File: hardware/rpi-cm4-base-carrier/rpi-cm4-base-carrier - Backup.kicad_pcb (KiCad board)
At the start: 4 copper layers, 129.5 x 61.3 mm, 66 parts, among them J1 690-019-298-412, J2 DNP, J3 USB4105-GF-A, J4 SM04B-SRSS-TB(LF)(SN), J5 THD-02-R, J6 Micro_SD_Card_Det, J7 USB_OTG, J8 690-008-221-904, J9 Conn_02x05_Odd_Even, U1 RT9742SNGV, U10 AP22653W6, U2 74LVC1G07SE-7, U3 TPD4EUSB30, U4 TPD4EUSB30, U5 MagJack-A70-112-331N126, U6 RT9742GGJ5, U7 FSUSB42MUX, U8 USB2514B-I/M2, U9 TPD4EUSB30, Y1 CX3225CA24000D0HSSCC

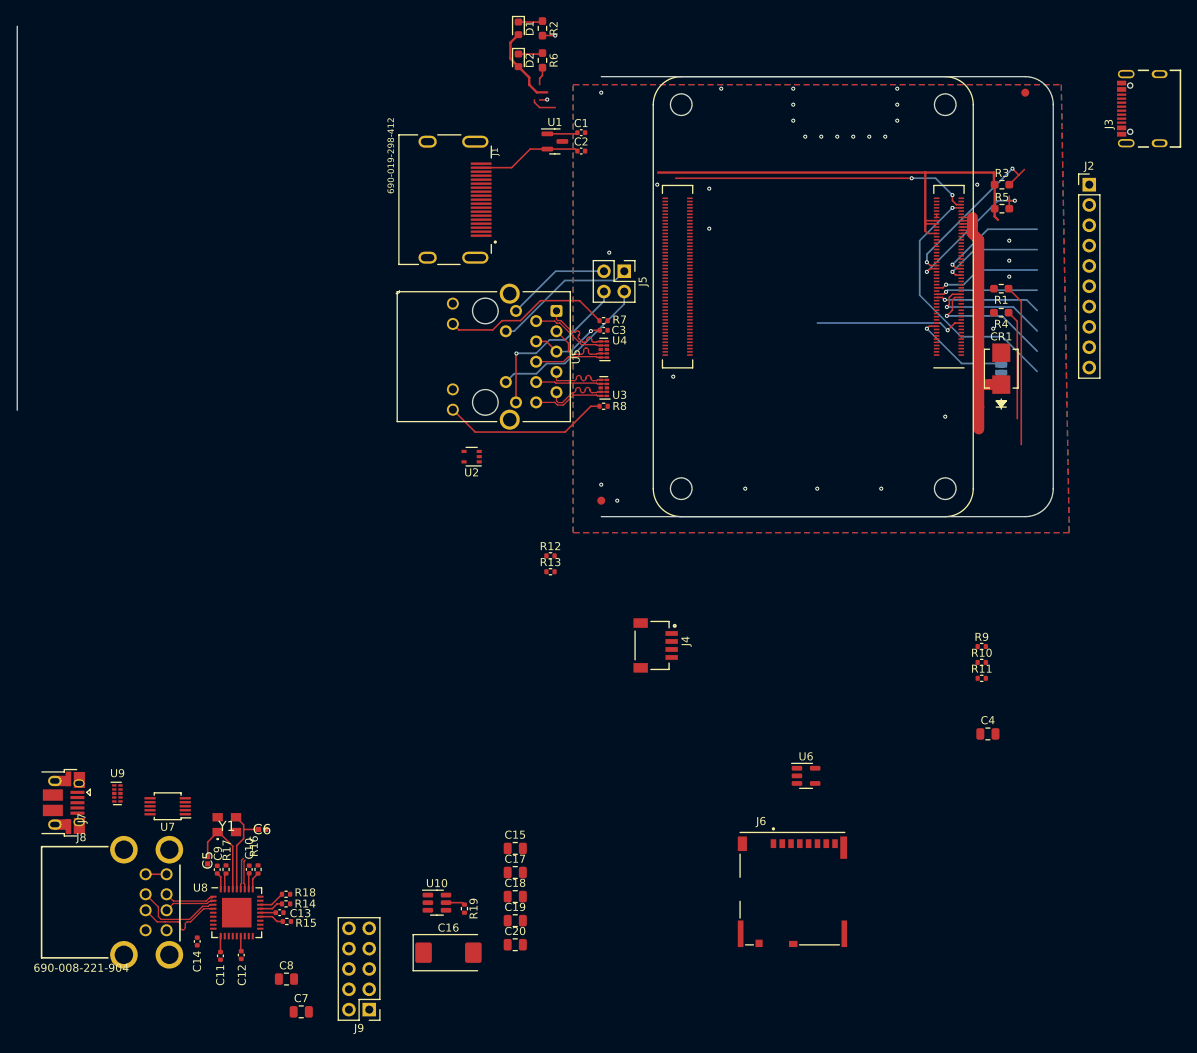
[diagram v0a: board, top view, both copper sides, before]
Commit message: routing for some modules progressing quickly, USBHUB mostly complete, thought needed regarding which connectors should be exposed post assembly and which should be for internal use only. LED identifiers and buttons still missing
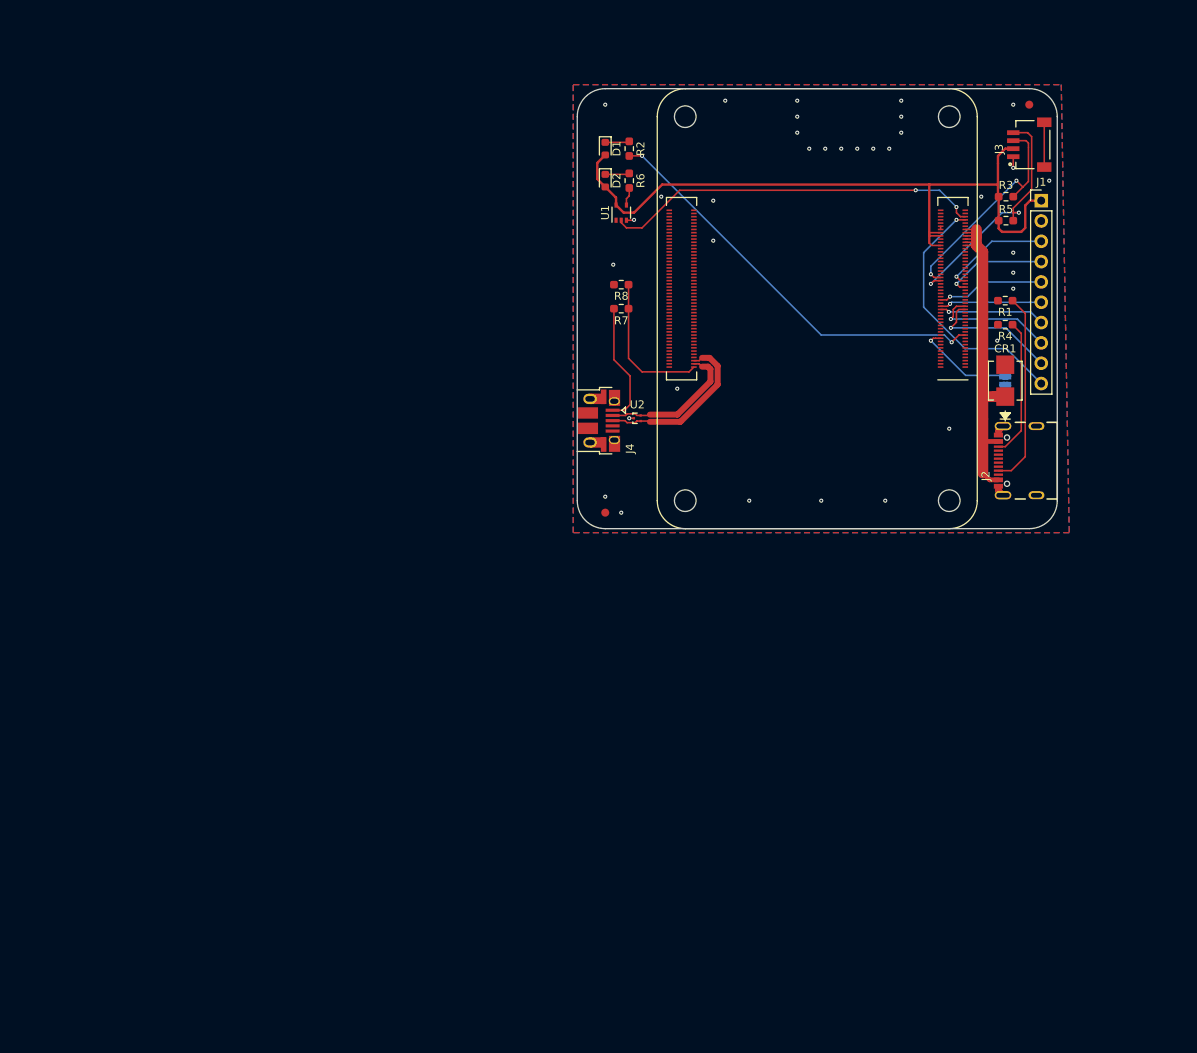
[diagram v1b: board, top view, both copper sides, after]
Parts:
- removed C1, C10, C11, C12, C13, C14, C2, C3, C9: 100n, Capacitor_SMD:C_0402_1005Metric
- removed C15, C17, C18, C19, C20, C4, C7, C8: 10u, Capacitor_SMD:C_0805_2012Metric
- removed C16: 100uF, Capacitor_Tantalum_SMD:CP_EIA-7343-31_Kemet-D
- removed C5, C6: 8pf, SamacSys_Parts:CAPC1005X56N
- removed J5: THD-02-R, Connector_PinHeader_2.54mm:PinHeader_2x02_P2.54mm_Vertical
- removed J6: Micro_SD_Card_Det, CM4IO:SDCARD_MOLEX_503398-1892
- removed J7: USB_OTG, CM4IO:USB_Micro-B_EDAC_UCON00686
- removed J8: 690-008-221-904, CM4IO:MOLEX_USB_67298-4090
- removed J9: Conn_02x05_Odd_Even, Connector_PinHeader_2.54mm:PinHeader_2x05_P2.54mm_Vertical
- removed R10, R9: nf, Resistor_SMD:R_0402_1005Metric
- removed R11, R17: 12K 1%, Resistor_SMD:R_0402_1005Metric
- removed R12, R13: 2.2K 1%, Resistor_SMD:R_0402_1005Metric
- removed R14, R15, R16, R18: 36K 1%, Resistor_SMD:R_0402_1005Metric
- removed R19: 15K 1%, Resistor_SMD:R_0402_1005Metric
- removed U10: AP22653W6, Package_TO_SOT_SMD:SOT-23-6
- removed U3, U4, U9: TPD4EUSB30, Package_SON:USON-10_2.5x1.0mm_P0.5mm
- removed U5: MagJack-A70-112-331N126, CM4IO:TRJG0926HENL
- removed U6: RT9742GGJ5, Package_TO_SOT_SMD:SOT-23-5
- removed U7: FSUSB42MUX, Package_SO:MSOP-10_3x3mm_P0.5mm
- removed U8: USB2514B-I/M2, Package_DFN_QFN:QFN-36-1EP_6x6mm_P0.5mm_EP3.7x3.7mm
- removed Y1: CX3225CA24000D0HSSCC, SamacSys_Parts:CX3225CA24000D0HSSCC
- J1: value 690-019-298-412 -> DNP; footprint CM4IO:EDAC 690-019-298-412 -> Connector_PinHeader_2.54mm:PinHeader_1x10_P2.54mm_Vertical
- J2: value DNP -> USB4105-GF-A; footprint Connector_PinHeader_2.54mm:PinHeader_1x10_P2.54mm_Vertical -> USB4105-GF-A:GCT_USB4105-GF-A
- J3: value USB4105-GF-A -> SM04B-SRSS-TB(LF)(SN); footprint USB4105-GF-A:GCT_USB4105-GF-A -> SM04B-SRSS-TB_LF__SN_:JST_SM04B-SRSS-TB(LF)(SN)
- J4: value SM04B-SRSS-TB(LF)(SN) -> USB_OTG; footprint SM04B-SRSS-TB_LF__SN_:JST_SM04B-SRSS-TB(LF)(SN) -> CM4IO:USB_Micro-B_EDAC_UCON00686
- R7, R8: value 470R -> 2.2K 1%; footprint Resistor_SMD:R_0402_1005Metric -> Resistor_SMD:R_0603_1608Metric_Pad0.98x0.95mm_HandSolder
- U1: value RT9742SNGV -> 74LVC1G07SE-7; footprint Package_TO_SOT_SMD:SOT-23 -> Package_TO_SOT_SMD:SOT-353_SC-70-5
- U2: value 74LVC1G07SE-7 -> TPD2EUSB30; footprint Package_TO_SOT_SMD:SOT-353_SC-70-5 -> Package_TO_SOT_SMD:Texas_DRT-3
- moved J1 70.7 mm to (174.5, 92.5), turned to 0 degrees
- moved J2 35.1 mm to (173.9, 125.0), turned to 90 degrees
- moved J4 29.9 mm to (118.1, 120.0)
- moved U2 21.2 mm to (124.0, 119.7), turned to 90 degrees
- moved J3 18.8 mm to (171.0, 85.5)
- moved D1 18.5 mm to (120.0, 86.0)
- moved D2 18.5 mm to (120.0, 90.0)
- moved R2 18.5 mm to (123.0, 86.0)
- moved R6 18.5 mm to (123.0, 90.0)
- moved R8 15.4 mm to (122.0, 103.0), turned to 180 degrees
- moved U1 12.2 mm to (122.0, 94.0), turned to 90 degrees
- moved R7 2.66 mm to (122.0, 106.0)
- moved CR1 1.58 mm to (170.0, 115.0)
- moved JP1 1.58 mm to (170.0, 115.0)
- moved Module1 1.58 mm to (163.0, 82.0)
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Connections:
- net /CM4 GPIO/SCL0 renamed Net-(Module1-Pad80)
- net /CM4 GPIO/SDA0 renamed Net-(Module1-Pad82)
- D1 pad 2: +3V3 -> +3.3V
- D2 pad 2: +3V3 -> +3.3V
- J1 pad 1: /CM4 High Speed/HDMI0_CK_N -> +3.3V
- J1 pad 10: /CM4 High Speed/HDMI0_CK_P -> /CM4 GPIO/nRPIBOOT
- J1 pad 3: /CM4 High Speed/HDMI0_CK_N -> /CM4 GPIO/GPIO14
- J1 pad 4: /CM4 High Speed/HDMI0_D1_P -> /CM4 GPIO/GPIO15
- J1 pad 5: GND -> /CM4 GPIO/GPIO10
- J1 pad 6: /CM4 High Speed/HDMI0_CK_N -> /CM4 GPIO/GPIO9
- J1 pad 7: /CM4 High Speed/HDMI0_D0_P -> /CM4 GPIO/GPIO11
- J1 pad 8: GND -> /CM4 GPIO/GPIO8
- J1 pad 9: /CM4 High Speed/HDMI0_D0_N -> /CM4 GPIO/GPIO7
- J4 pad 1: GND -> Net-(J4-Pad1)
- J4 pad 2: +3V3 -> /CM4 High Speed/USB2_N
- J4 pad 3: /CM4 GPIO/GPIO2 -> /CM4 High Speed/USB2_P
- J4 pad 4: /CM4 GPIO/GPIO3 -> Net-(J4-Pad4)
- Module1 pad 10: /CM4 GPIO/TRD0_N -> Net-(Module1-Pad10)
- Module1 pad 100: /CM4 High Speed/USB2-HUB/nEXTRST -> Net-(Module1-Pad100)
- Module1 pad 102: unconnected-(Module1B-PCIe_CLK_nREQ-Pad102) -> Net-(Module1-Pad102)
- Module1 pad 104: unconnected-(Module1B-Reserved-Pad104) -> Net-(Module1-Pad104)
- Module1 pad 105: /CM4 High Speed/USB2_N -> /CM4 High Speed/USB2_P
- Module1 pad 106: unconnected-(Module1B-Reserved-Pad106) -> Net-(Module1-Pad106)
- Module1 pad 109: unconnected-(Module1B-PCIe_nRST-Pad109) -> Net-(Module1-Pad109)
- Module1 pad 11: /CM4 GPIO/TRD2_P -> Net-(Module1-Pad11)
- Module1 pad 110: unconnected-(Module1B-PCIe_CLK_P-Pad110) -> Net-(Module1-Pad110)
- Module1 pad 111: unconnected-(Module1B-VDAC_COMP-Pad111) -> Net-(Module1-Pad111)
- Module1 pad 112: unconnected-(Module1B-PCIe_CLK_N-Pad112) -> Net-(Module1-Pad112)
- Module1 pad 115: unconnected-(Module1B-CAM1_D0_N-Pad115) -> Net-(Module1-Pad115)
- Module1 pad 116: unconnected-(Module1B-PCIe_RX_P-Pad116) -> Net-(Module1-Pad116)
- Module1 pad 117: unconnected-(Module1B-CAM1_D0_P-Pad117) -> Net-(Module1-Pad117)
- Module1 pad 118: unconnected-(Module1B-PCIe_RX_N-Pad118) -> Net-(Module1-Pad118)
- Module1 pad 12: /CM4 GPIO/TRD0_P -> Net-(Module1-Pad12)
- Module1 pad 121: unconnected-(Module1B-CAM1_D1_N-Pad121) -> Net-(Module1-Pad121)
- Module1 pad 122: unconnected-(Module1B-PCIe_TX_P-Pad122) -> Net-(Module1-Pad122)
- Module1 pad 123: unconnected-(Module1B-CAM1_D1_P-Pad123) -> Net-(Module1-Pad123)
- Module1 pad 124: unconnected-(Module1B-PCIe_TX_N-Pad124) -> Net-(Module1-Pad124)
- Module1 pad 127: unconnected-(Module1B-CAM1_C_N-Pad127) -> Net-(Module1-Pad127)
- Module1 pad 128: unconnected-(Module1B-CAM0_D0_N-Pad128) -> Net-(Module1-Pad128)
- Module1 pad 129: unconnected-(Module1B-CAM1_C_P-Pad129) -> Net-(Module1-Pad129)
- Module1 pad 130: unconnected-(Module1B-CAM0_D0_P-Pad130) -> Net-(Module1-Pad130)
- Module1 pad 133: unconnected-(Module1B-CAM1_D2_N-Pad133) -> Net-(Module1-Pad133)
- Module1 pad 134: unconnected-(Module1B-CAM0_D1_N-Pad134) -> Net-(Module1-Pad134)
- Module1 pad 135: unconnected-(Module1B-CAM1_D2_P-Pad135) -> Net-(Module1-Pad135)
- Module1 pad 136: unconnected-(Module1B-CAM0_D1_P-Pad136) -> Net-(Module1-Pad136)
- Module1 pad 139: unconnected-(Module1B-CAM1_D3_N-Pad139) -> Net-(Module1-Pad139)
- Module1 pad 140: unconnected-(Module1B-CAM0_C_N-Pad140) -> Net-(Module1-Pad140)
- Module1 pad 141: unconnected-(Module1B-CAM1_D3_P-Pad141) -> Net-(Module1-Pad141)
- Module1 pad 142: unconnected-(Module1B-CAM0_C_P-Pad142) -> Net-(Module1-Pad142)
- Module1 pad 143: unconnected-(Module1B-HDMI1_HOTPLUG-Pad143) -> Net-(Module1-Pad143)
- Module1 pad 145: unconnected-(Module1B-HDMI1_SDA-Pad145) -> Net-(Module1-Pad145)
- Module1 pad 146: unconnected-(Module1B-HDMI1_TX2_P-Pad146) -> Net-(Module1-Pad146)
- Module1 pad 147: unconnected-(Module1B-HDMI1_SCL-Pad147) -> Net-(Module1-Pad147)
- Module1 pad 148: unconnected-(Module1B-HDMI1_TX2_N-Pad148) -> Net-(Module1-Pad148)
- Module1 pad 149: unconnected-(Module1B-HDMI1_CEC-Pad149) -> Net-(Module1-Pad149)
- Module1 pad 15: /CM4 GPIO/ETH_LEDY -> Net-(Module1-Pad15)
- Module1 pad 151: unconnected-(Module1B-HDMI0_CEC-Pad151) -> Net-(Module1-Pad151)
- Module1 pad 152: unconnected-(Module1B-HDMI1_TX1_P-Pad152) -> Net-(Module1-Pad152)
- Module1 pad 153: /CM4 High Speed/HDMI0_HOTPLUG -> Net-(Module1-Pad153)
- Module1 pad 154: unconnected-(Module1B-HDMI1_TX1_N-Pad154) -> Net-(Module1-Pad154)
- Module1 pad 157: unconnected-(Module1B-DSI0_D0_N-Pad157) -> Net-(Module1-Pad157)
- Module1 pad 158: unconnected-(Module1B-HDMI1_TX0_P-Pad158) -> Net-(Module1-Pad158)
- Module1 pad 159: unconnected-(Module1B-DSI0_D0_P-Pad159) -> Net-(Module1-Pad159)
- Module1 pad 16: unconnected-(Module1A-Ethernet_SYNC_IN(1.8v)-Pad16) -> Net-(Module1-Pad16)
- Module1 pad 160: unconnected-(Module1B-HDMI1_TX0_N-Pad160) -> Net-(Module1-Pad160)
- Module1 pad 163: unconnected-(Module1B-DSI0_D1_N-Pad163) -> Net-(Module1-Pad163)
- Module1 pad 164: unconnected-(Module1B-HDMI1_CLK_P-Pad164) -> Net-(Module1-Pad164)
- Module1 pad 165: unconnected-(Module1B-DSI0_D1_P-Pad165) -> Net-(Module1-Pad165)
- Module1 pad 166: unconnected-(Module1B-HDMI1_CLK_N-Pad166) -> Net-(Module1-Pad166)
- Module1 pad 169: unconnected-(Module1B-DSI0_C_N-Pad169) -> Net-(Module1-Pad169)
- Module1 pad 17: /CM4 GPIO/ETH_LEDG -> Net-(Module1-Pad17)
- Module1 pad 170: /CM4 High Speed/HDMI0_CK_N -> Net-(Module1-Pad170)
- Module1 pad 171: unconnected-(Module1B-DSI0_C_P-Pad171) -> Net-(Module1-Pad171)
- Module1 pad 172: /CM4 High Speed/HDMI0_CK_N -> Net-(Module1-Pad172)
- Module1 pad 175: unconnected-(Module1B-DSI1_D0_N-Pad175) -> Net-(Module1-Pad175)
- Module1 pad 176: /CM4 High Speed/HDMI0_D1_P -> Net-(Module1-Pad176)
- Module1 pad 177: unconnected-(Module1B-DSI1_D0_P-Pad177) -> Net-(Module1-Pad177)
- Module1 pad 178: /CM4 High Speed/HDMI0_CK_N -> Net-(Module1-Pad178)
- Module1 pad 18: unconnected-(Module1A-Ethernet_SYNC_OUT(1.8v)-Pad18) -> Net-(Module1-Pad18)
- Module1 pad 181: unconnected-(Module1B-DSI1_D1_N-Pad181) -> Net-(Module1-Pad181)
- Module1 pad 182: /CM4 High Speed/HDMI0_D0_P -> Net-(Module1-Pad182)
- Module1 pad 183: unconnected-(Module1B-DSI1_D1_P-Pad183) -> Net-(Module1-Pad183)
- Module1 pad 184: /CM4 High Speed/HDMI0_D0_N -> Net-(Module1-Pad184)
- Module1 pad 187: unconnected-(Module1B-DSI1_C_N-Pad187) -> Net-(Module1-Pad187)
- Module1 pad 188: /CM4 High Speed/HDMI0_CK_P -> Net-(Module1-Pad188)
- Module1 pad 189: unconnected-(Module1B-DSI1_C_P-Pad189) -> Net-(Module1-Pad189)
- Module1 pad 19: unconnected-(Module1A-Ethernet_nLED1(3.3v)-Pad19) -> Net-(Module1-Pad19)
- Module1 pad 190: /CM4 High Speed/HDMI0_CK_N -> Net-(Module1-Pad190)
- Module1 pad 193: unconnected-(Module1B-DSI1_D2_N-Pad193) -> Net-(Module1-Pad193)
- Module1 pad 194: unconnected-(Module1B-DSI1_D3_N-Pad194) -> Net-(Module1-Pad194)
- Module1 pad 195: unconnected-(Module1B-DSI1_D2_P-Pad195) -> Net-(Module1-Pad195)
- Module1 pad 196: unconnected-(Module1B-DSI1_D3_P-Pad196) -> Net-(Module1-Pad196)
- Module1 pad 199: /CM4 High Speed/HDMI0_SDA -> Net-(Module1-Pad199)
- Module1 pad 200: /CM4 High Speed/HDMI0_SCL -> Net-(Module1-Pad200)
- Module1 pad 24: unconnected-(Module1A-GPIO26-Pad24) -> Net-(Module1-Pad24)
- Module1 pad 25: unconnected-(Module1A-GPIO21-Pad25) -> Net-(Module1-Pad25)
- Module1 pad 26: unconnected-(Module1A-GPIO19-Pad26) -> Net-(Module1-Pad26)
- Module1 pad 27: unconnected-(Module1A-GPIO20-Pad27) -> Net-(Module1-Pad27)
- Module1 pad 28: unconnected-(Module1A-GPIO13-Pad28) -> Net-(Module1-Pad28)
- Module1 pad 29: unconnected-(Module1A-GPIO16-Pad29) -> Net-(Module1-Pad29)
- Module1 pad 3: /CM4 GPIO/TRD3_P -> Net-(Module1-Pad3)
- Module1 pad 30: unconnected-(Module1A-GPIO6-Pad30) -> Net-(Module1-Pad30)
- Module1 pad 31: unconnected-(Module1A-GPIO12-Pad31) -> Net-(Module1-Pad31)
- Module1 pad 34: unconnected-(Module1A-GPIO5-Pad34) -> Net-(Module1-Pad34)
- Module1 pad 35: unconnected-(Module1A-ID_SC-Pad35) -> Net-(Module1-Pad35)
- Module1 pad 36: unconnected-(Module1A-ID_SD-Pad36) -> Net-(Module1-Pad36)
- Module1 pad 4: /CM4 GPIO/TRD1_P -> Net-(Module1-Pad4)
- Module1 pad 41: unconnected-(Module1A-GPIO25-Pad41) -> Net-(Module1-Pad41)
- Module1 pad 45: unconnected-(Module1A-GPIO24-Pad45) -> Net-(Module1-Pad45)
- Module1 pad 46: unconnected-(Module1A-GPIO22-Pad46) -> Net-(Module1-Pad46)
- Module1 pad 47: unconnected-(Module1A-GPIO23-Pad47) -> Net-(Module1-Pad47)
- Module1 pad 48: unconnected-(Module1A-GPIO27-Pad48) -> Net-(Module1-Pad48)
- Module1 pad 49: unconnected-(Module1A-GPIO18-Pad49) -> Net-(Module1-Pad49)
- Module1 pad 5: /CM4 GPIO/TRD3_N -> Net-(Module1-Pad5)
- Module1 pad 50: unconnected-(Module1A-GPIO17-Pad50) -> Net-(Module1-Pad50)
- Module1 pad 54: unconnected-(Module1A-GPIO4-Pad54) -> Net-(Module1-Pad54)
- Module1 pad 57: /CM4 GPIO/SD_CLK -> Net-(Module1-Pad57)
- Module1 pad 6: /CM4 GPIO/TRD1_N -> Net-(Module1-Pad6)
- Module1 pad 61: /CM4 GPIO/SD_DAT3 -> Net-(Module1-Pad61)
- Module1 pad 62: /CM4 GPIO/SD_CMD -> Net-(Module1-Pad62)
- Module1 pad 63: /CM4 GPIO/SD_DAT0 -> Net-(Module1-Pad63)
- Module1 pad 64: unconnected-(Module1A-SD_DAT5-Pad64) -> Net-(Module1-Pad64)
- Module1 pad 67: /CM4 GPIO/SD_DAT1 -> Net-(Module1-Pad67)
- Module1 pad 68: unconnected-(Module1A-SD_DAT4-Pad68) -> Net-(Module1-Pad68)
- Module1 pad 69: /CM4 GPIO/SD_DAT2 -> Net-(Module1-Pad69)
- Module1 pad 70: unconnected-(Module1A-SD_DAT7-Pad70) -> Net-(Module1-Pad70)
- Module1 pad 72: unconnected-(Module1A-SD_DAT6-Pad72) -> Net-(Module1-Pad72)
- Module1 pad 73: unconnected-(Module1A-SD_VDD_Override-Pad73) -> Net-(Module1-Pad73)
- Module1 pad 75: /CM4 GPIO/SD_PWR_ON -> Net-(Module1-Pad75)
- Module1 pad 76: unconnected-(Module1A-Reserved-Pad76) -> Net-(Module1-Pad76)
- Module1 pad 78: +3V3 -> +3.3V
- Module1 pad 84: +3V3 -> +3.3V
- Module1 pad 86: +3V3 -> +3.3V
- Module1 pad 88: +3V3 -> +1.8V
- Module1 pad 89: unconnected-(Module1A-WiFi_nDisable-Pad89) -> Net-(Module1-Pad89)
- Module1 pad 9: /CM4 GPIO/TRD2_N -> Net-(Module1-Pad9)
- Module1 pad 90: +3V3 -> +1.8V
- Module1 pad 91: unconnected-(Module1A-BT_nDisable-Pad91) -> Net-(Module1-Pad91)
- Module1 pad 92: unconnected-(Module1A-RUN_PG-Pad92) -> Net-(Module1-Pad92)
- Module1 pad 94: unconnected-(Module1A-AnalogIP0-Pad94) -> Net-(Module1-Pad94)
- Module1 pad 96: unconnected-(Module1A-AnalogIP1-Pad96) -> Net-(Module1-Pad96)
- Module1 pad 97: unconnected-(Module1A-Camera_GPIO-Pad97) -> Net-(Module1-Pad97)
- Module1 pad 99: unconnected-(Module1A-Global_EN-Pad99) -> Net-(Module1-Pad99)
- R1 pad 1: Net-(J3-CC1) -> Net-(J2-PadA5)
- R3 pad 1: +3V3 -> +3.3V
- R4 pad 1: Net-(J3-CC2) -> Net-(J2-PadB5)
- R5 pad 1: +3V3 -> +3.3V
- R7 pad 1: Net-(U5-LEDG_K) -> Net-(J4-Pad1)
- R7 pad 2: /CM4 GPIO/ETH_LEDG -> /CM4 High Speed/USB_OTG_ID
- R8 pad 1: Net-(U5-LEDY_K) -> /CM4 High Speed/USB_OTG_ID
- R8 pad 2: /CM4 GPIO/ETH_LEDY -> GND
- U1 pad 1: +5V -> (no net)
- U1 pad 2: /CM4 High Speed/HDMI/HDMI_5v -> /CM4 GPIO/nPWR_LED
- U2 pad 1: (no net) -> /CM4 High Speed/USB2_P
- U2 pad 2: /CM4 GPIO/nPWR_LED -> /CM4 High Speed/USB2_N
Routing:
- net +3.3V: track 0.00 -> 89.7 mm
- net +3V3: track 80.5 -> 0.00 mm
- net /CM4 GPIO/nLED_Activity: track 20.4 -> 52.0 mm
- net Net-(J2-PadA5): track 0.00 -> 24.2 mm
- net Net-(U5-LEDG_K): track 21.2 -> 0.00 mm
- net /CM4 High Speed/USB2_P: track 0.00 -> 21.1 mm
- net /magjack/TR3_TAP: track 21.0 -> 0.00 mm, vias 1 -> 0
- net Net-(U5-LEDY_K): track 20.8 -> 0.00 mm
- net /magjack/TR2_TAP: track 20.4 -> 0.00 mm
- net Net-(J3-CC1): track 20.2 -> 0.00 mm
- net /CM4 High Speed/USB_OTG_ID: track 0.00 -> 18.3 mm
- net /CM4 High Speed/USB2_N: track 0.00 -> 18.1 mm
- net /magjack/TR1_TAP: track 17.9 -> 0.00 mm
- net Net-(J2-PadB5): track 0.00 -> 17.4 mm
- net Net-(J4-Pad1): track 0.00 -> 15.3 mm
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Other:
- board size 129.5 x 61.3 mm -> 60 x 55 mm
- copper layers 4 -> 2
- rule pad_to_mask_clearance: 0.05 -> 0
